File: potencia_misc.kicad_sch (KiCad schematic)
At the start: 68 parts, among them J6 ATX-20, M1 Fan, M2 Fan, M3 Fan, Q1 NMOS, Q10 MMBT2222A, Q11 MMBT2222A, Q12 MMBT2222A, Q13 MMBT2222A, Q14 MMBT2907ALT1G, Q15 MMBT2222A, Q16 MMBT2222A, Q17 MMBT2222A, Q18 MMBT2907ALT1G, Q19 MMBT2222A, Q2 NMOS, Q20 MMBT2907ALT1G, Q3 NMOS, Q4 NMOS, Q9 MMBT2907ALT1G, SW3 SW_Push, U8 TPS54302

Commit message: 10082026/B
nova revisão
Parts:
- removed C59: 10uf, symbol Device:C
- removed C60, C62: 100nf, Capacitor_SMD:C_0603_1608Metric, symbol Device:C
- removed C66, C67: 22µf, Capacitor_SMD:C_0603_1608Metric, symbol Device:C
- removed C93: 47µf, Capacitor_SMD:C_0603_1608Metric_Pad1.08x0.95mm_HandSolder, symbol Device:C
- removed D1: SMF15A, Diode_SMD:D_SMF, symbol Diode:SMF15A
- removed D2: SMF33A, Diode_SMD:D_SMF, symbol Diode:SMF33A
- removed F1: Polyfuse, symbol Device:Polyfuse
- removed J6: ATX-20, Connector_Molex:Molex_Mini-Fit_Jr_5566-20A_2x10_P4.20mm_Vertical, symbol Connector:ATX-20
- removed L1: 6.8uh, Inductor_SMD:L_Bourns_SRP1038C_10.0x10.0mm, symbol Device:L
- removed R42: 100k, symbol Device:R
- removed R43: 22k, symbol Device:R
- removed TP12: TestPoint, TestPoint:TestPoint_Pad_D1.0mm, symbol Connector:TestPoint
- removed U8: TPS54302, Package_TO_SOT_SMD:SOT-23-6, symbol Regulator_Switching:TPS54302
- added C100, C101: 100nf, Capacitor_SMD:C_0603_1608Metric, symbol Device:C
- added C15: 100nf, symbol Device:C_Small
- added C31: 33nf, Capacitor_SMD:C_0402_1005Metric, symbol Device:C_Small
- added C49, C51, C97, C98: 22µf, symbol Device:C
- added D6: SMF33A, Diode_SMD:D_SMF, symbol Diode:SMF33A
- added F9: Polyfuse, symbol Device:Polyfuse
- added J6: ATX-24, Connector_Molex:Molex_Mini-Fit_Jr_5569-24A2_2x12_P4.20mm_Horizontal, symbol Connector:ATX-24
- added JP5: fre, Jumper:SolderJumper-2_P1.3mm_Open_TrianglePad1.0x1.5mm, symbol Jumper:SolderJumper_2_Open
- added L2: 4.7µh, symbol Device:L
- added R88: 100kΩ, symbol Device:R
- added R89: 57.6kΩ, symbol Device:R
- added R90: 10kΩ, symbol Device:R
- added R92: 330, symbol Device:R_Small
- added R93: 30.9kΩ, symbol Device:R_Small
- added U9: TPS62933F, Package_TO_SOT_SMD:SOT-583-8, symbol Regulator_Switching:TPS62933F
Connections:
- net +12V: now also F9.1
- net +3.3V: now also D6.1 (A1)
- net GND: now also C100.2, C101.2, C31.2, C49.2, C51.2, C97.2, C98.2, D6.2 (A2), J6.15 (GND), J6.17 (GND), J6.18 (GND), J6.19 (GND), J6.24 (GND), J6.3 (GND), J6.5 (GND), J6.7 (GND), JP5.1 (A), R89.2, R90.2, U9.4 (GND)
- net SUB_1: now also J6.16 (PS_ON#)
- net hotbed: now also J6.10 (+12V), J6.11 (+12V)
- net at F3.1: now also J6.21 (+5V), J6.22 (+5V), J6.23 (+5V), J6.4 (+5V), J6.6 (+5V)
- new net: R88.2, R89.1, U9.2 (EN)
- new net: C31.1, U9.7 (SS)
- new net: C15.1, U9.6 (BST)
- new net: C15.2, L2.1, U9.5 (SW)
- new net: C101.1, C49.1, C51.1, F9.2, R88.1, U9.3 (VIN)
- new net: JP5.2 (B), U9.1 (RT)
- new net: R92.2, R93.1
- new net: R90.1, R93.2, U9.8 (FB)
- new net: C100.1, C97.1, C98.1, L2.2, R92.1
- new net: J6.1 (+3.3V), J6.12 (+3.3V), J6.13 (+3.3V), J6.2 (+3.3V)
- no-connect marks 5 -> 4
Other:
- company: (none) -> ---
- moved on the sheet: C61, C63, C64, C65, C94, F2, F3, SW3, TP11, TP13, TP14, TP15

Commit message: 10082026/D
"erros bobos"
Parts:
- removed Q10, Q11, Q12, Q13, Q15, Q16, Q17, Q19: MMBT2222A, Package_TO_SOT_SMD:SOT-23, symbol Transistor_BJT:MMBT2222A
- removed Q14, Q18, Q20, Q9: MMBT2907ALT1G, Package_TO_SOT_SMD:SOT-23, symbol Simulation_SPICE:PNP
- removed R76, R81, R86, R87: 39Ω, symbol Device:R
- removed R77, R78, R79, R80, R82, R83, R84, R85: 1kΩ, symbol Device:R
- added C10, C12, C8, C9: 100nf, symbol Device:C
- added Q10, Q11, Q12, Q9: PMOS, symbol Simulation_SPICE:PMOS
- added Q22, Q23, Q24, Q25: NMOS, symbol Simulation_SPICE:NMOS
- added R100, R104, R108, R112: 100, symbol Device:R
- added R101, R105, R109, R113: 220, symbol Device:R
- added R102, R106, R110, R98: 100Ω, symbol Device:R
- added R103, R107, R111, R99: 10k, symbol Device:R
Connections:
- net Fan_2_D is gone; now on net Fan_1_D: Q4.2 (G), R47.1
- net exrtusora_out is gone; now on net Fan_1_D: Q2.2 (G), R45.1
- net +12V: now also R100.2, R104.2, R108.2, R112.2
- net +3.3V: now also C100.1, C97.1, C98.1, L2.2, R92.1
- net Fan_1: now also Q11.2 (G), Q24.2 (G), R106.1, R107.1
- net Fan_1_D: now also C10.2, C12.2, C8.2, C9.2, Q10.3 (S), Q11.3 (S), Q12.3 (S), Q22.1 (D), Q23.1 (D), Q24.1 (D), Q25.1 (D), Q9.3 (S), R101.2, R105.2, R109.2, R113.2
- net Fan_2: now also Q12.2 (G), Q25.2 (G), R110.1, R111.1
- net GND: now also C10.1, C12.1, C8.1, C9.1, Q22.3 (S), Q23.3 (S), Q24.3 (S), Q25.3 (S), R101.1, R102.2, R103.2, R105.1, R106.2, R107.2, R109.1, R110.2, R111.2, R113.1, R98.2, R99.2
- net exrtusora: now also Q10.2 (G), Q23.2 (G), R102.1, R103.1
- net hot_bed: now also Q22.2 (G), Q9.2 (G), R98.1, R99.1
- new net: Q12.1 (D), R112.1
- new net: Q10.1 (D), R104.1
- new net: Q11.1 (D), R108.1
- new net: Q9.1 (D), R100.1
- no-connect marks 4 -> 5

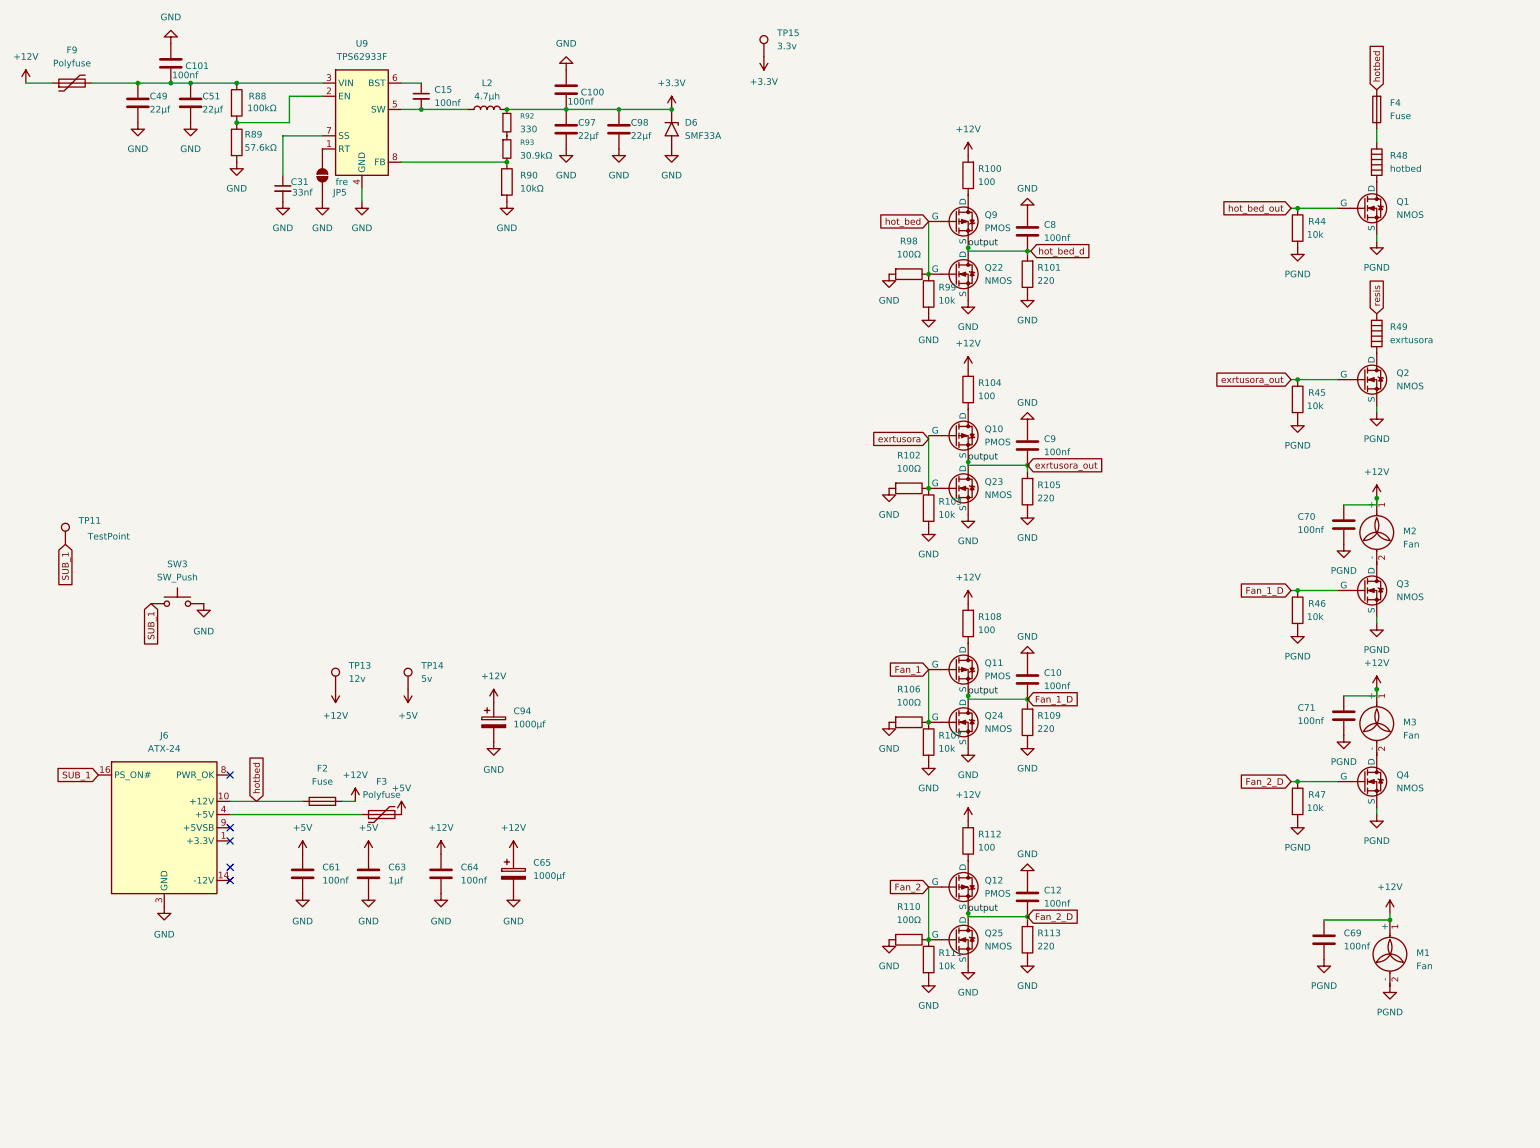
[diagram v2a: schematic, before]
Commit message: 17082026/E
modulo FRAM e Melhoria no esquemático
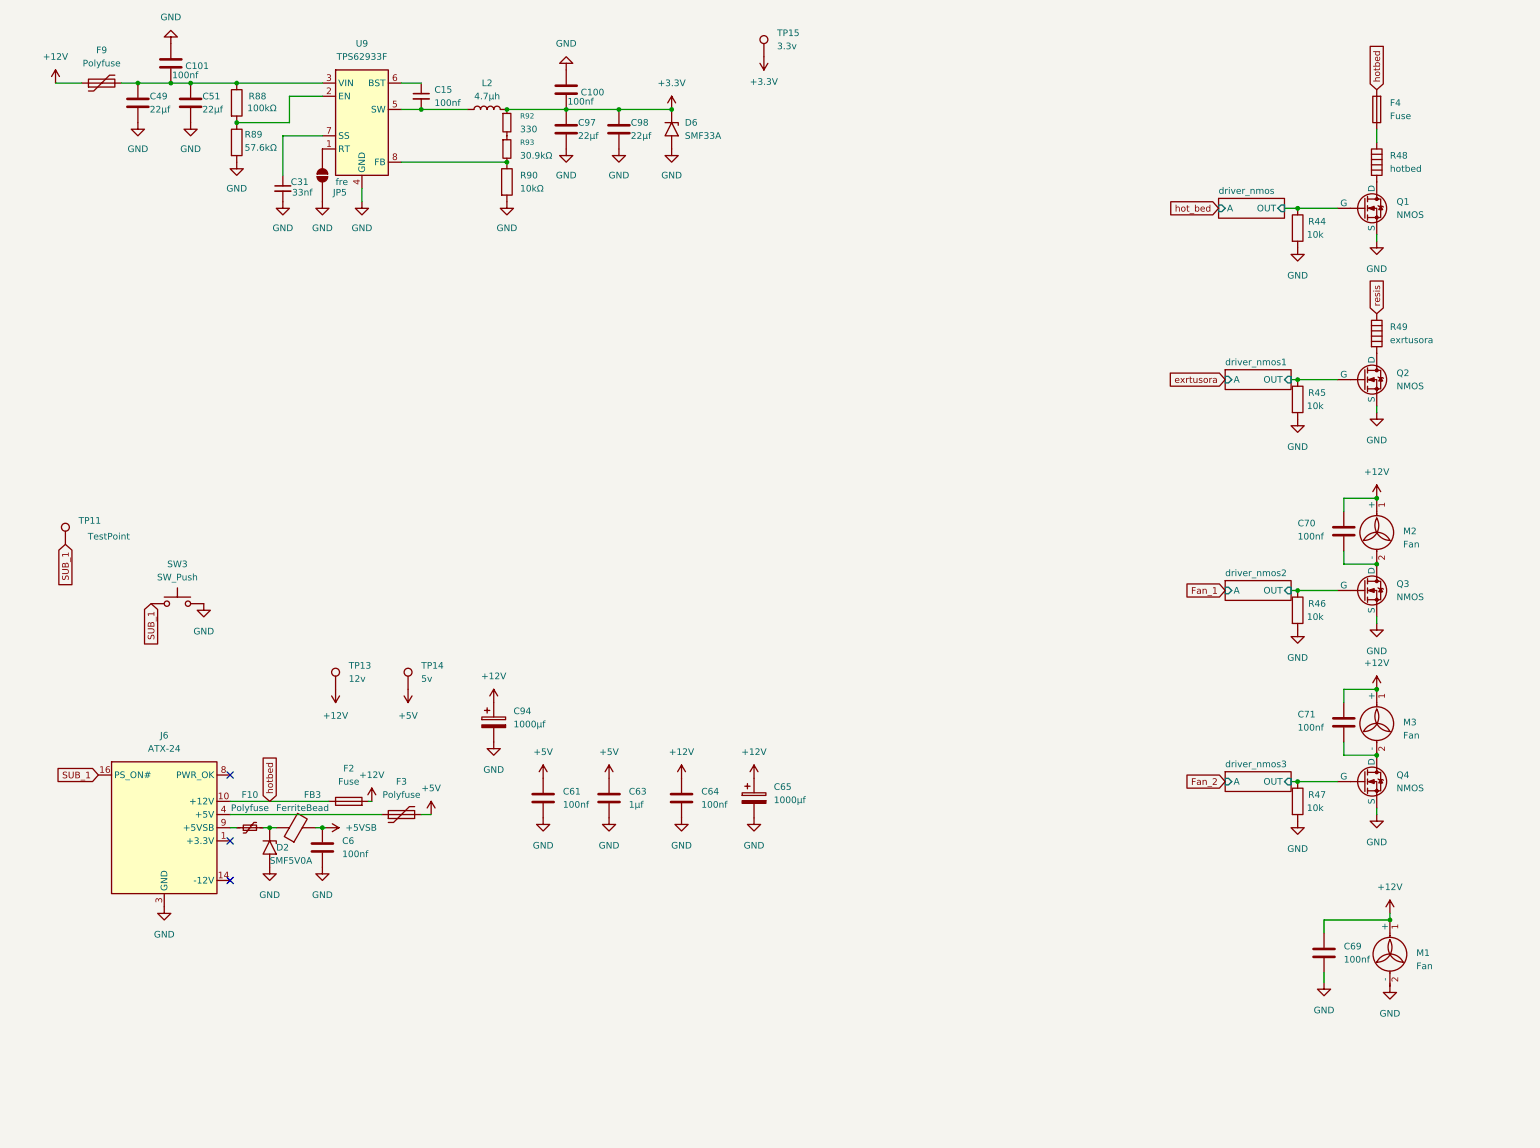
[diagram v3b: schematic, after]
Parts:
- removed C10, C12, C8, C9: 100nf, symbol Device:C
- removed Q10, Q11, Q12, Q9: PMOS, symbol Simulation_SPICE:PMOS
- removed Q22, Q23, Q24, Q25: NMOS, symbol Simulation_SPICE:NMOS
- removed R100, R104, R108, R112: 100, symbol Device:R
- removed R101, R105, R109, R113: 220, symbol Device:R
- removed R102, R106, R110, R98: 100Ω, symbol Device:R
- removed R103, R107, R111, R99: 10k, symbol Device:R
- added C6: 100nf, Capacitor_SMD:C_0603_1608Metric, symbol Device:C
- added D2: SMF5V0A, Diode_SMD:D_SMF, symbol Diode:SMF5V0A
- added F10: Polyfuse, symbol Device:Polyfuse_Small
- added FB3: FerriteBead, Inductor_SMD:L_0805_2012Metric, symbol Device:FerriteBead
- C15: footprint (none) -> Capacitor_SMD:C_0603_1608Metric; jlc_pcb: (none) -> C346191
- C63: footprint (none) -> Capacitor_SMD:C_0805_2012Metric_Pad1.18x1.45mm_HandSolder; jlc_pcb: (none) -> C28323
- J6: Descrição (none) -> entrada de alimentaçao para o harpia ninho 12v, os pinos na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
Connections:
- net GND: now also C69.2, M1.2 (-), Q1.3 (S), Q2.3 (S), Q3.3 (S), Q4.3 (S), R44.2, R45.2, R46.2, R47.2, C6.2, D2.2 (A2)
- net at M2.2 (-), Q3.1 (D): now also C70.2
- net at M3.2 (-), Q4.1 (D): now also C71.2
- net at J6.9 (+5VSB): now also F10.1
- removed net Fan_1_D: Q2.2 (G), Q3.2 (G), Q4.2 (G), R45.1, R46.1, R47.1
- removed net PGND: C69.2, C70.2, C71.2, M1.2 (-), Q1.3 (S), Q2.3 (S), Q3.3 (S), Q4.3 (S), R44.2, R45.2, R46.2, R47.2
- net hot_bed_out renamed driver_nmos/OUT
- new net: D2.1 (A1), F10.2, FB3.1
- new net +5VSB: C6.1, FB3.2
- new net driver_nmos1/OUT: Q2.2 (G), R45.1
- new net driver_nmos2/OUT: Q3.2 (G), R46.1
- new net driver_nmos3/OUT: Q4.2 (G), R47.1
- no-connect marks 5 -> 3
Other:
- added sheet driver_nmos (d-nmos.kicad_sch)
- added sheet driver_nmos1 (d-nmos.kicad_sch)
- added sheet driver_nmos2 (d-nmos.kicad_sch)
- added sheet driver_nmos3 (d-nmos.kicad_sch)
- moved on the sheet: C61, C63, C64, C65, C69, C70, C71, F2, F3, F9

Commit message: 18082026/F
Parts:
- removed D6: SMF33A, Diode_SMD:D_SMF, symbol Diode:SMF33A
- added D7: SMF5V0A, Diode_SMD:D_SMF, symbol Diode:SMF5V0A
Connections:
- net +3.3V: now also D7.1 (A1)
- net GND: now also D7.2 (A2)
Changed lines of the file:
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@@
-	)
-	(symbol
-		(lib_id "Diode:SMF33A")
-		(at 139.7 33.02 270)
-		(unit 1)
-		(body_style 1)
-		(exclude_from_sim no)
-		(in_bom yes)
-		(on_board yes)
-		(in_pos_files yes)
-		(dnp no)
-		(fields_autoplaced yes)
-		(property "Reference" "D6"
-			(at 142.24 31.7499 90)
-			(show_name no)
-			(do_not_autoplace no)
-			(effects
-				(font
-					(size 1.27 1.27)
-				)
-				(justify left)
-			)
-		)
-		(property "Value" "SMF33A"
-			(at 142.24 34.2899 90)
-			(show_name no)
-			(do_not_autoplace no)
-			(effects
-				(font
-					(size 1.27 1.27)
-				)
-				(justify left)
-			)
-		)
-		(property "Footprint" "Diode_SMD:D_SMF"
-			(at 134.62 33.02 0)
-			(hide yes)
-			(show_name no)
-			(do_not_autoplace no)
-			(effects
-				(font
-					(size 1.27 1.27)
-				)
-			)
-		)
-		(property "Datasheet" "https://www.vishay.com/doc?85881"
-			(at 139.7 31.75 0)
-			(hide yes)
-			(show_name no)
-			(do_not_autoplace no)
-			(effects
-				(font
-					(size 1.27 1.27)
-				)
-			)
-		)
-		(property "Description" "200W unidirectional Transil Transient Voltage Suppressor, 33Vrwm, SMF"
-			(at 139.7 33.02 0)
-			(hide yes)
-			(show_name no)
-			(do_not_autoplace no)
-			(effects
-				(font
-					(size 1.27 1.27)
-				)
-			)
-		)
-		(pin "1"
-		)
-		(pin "2"
-		)
-		(instances
-			(project "hapia"
-				(path "/a3449e8f-77d7-48cf-b22a-69e9391d97ed"
-					(reference "D6")
-					(unit 1)
-				)
-			)
-		)
 	)
 	(symbol
@@
 					(unit 1)
 				)
+			)
+		)
+	)
+	(symbol
+		(lib_id "Diode:SMF5V0A")
+		(at 139.7 33.02 270)
+		(unit 1)
+		(body_style 1)
+		(exclude_from_sim no)
+		(in_bom yes)
+		(on_board yes)
+		(in_pos_files yes)
+		(dnp no)
+		(fields_autoplaced yes)
+		(property "Reference" "D7"
+			(at 142.24 31.7499 90)
+			(show_name no)
+			(do_not_autoplace no)
+			(effects
+				(font
+					(size 1.27 1.27)
+				)
+				(justify left)
+			)
+		)
+		(property "Value" "SMF5V0A"
+			(at 142.24 34.2899 90)
+			(show_name no)
+			(do_not_autoplace no)
+			(effects
+				(font
+					(size 1.27 1.27)
+				)
+				(justify left)
+			)
+		)
+		(property "Footprint" "Diode_SMD:D_SMF"
+			(at 134.62 33.02 0)
+			(hide yes)
+			(show_name no)
+			(do_not_autoplace no)
+			(effects
+				(font
+					(size 1.27 1.27)
+				)
+			)
+		)
+		(property "Datasheet" "https://www.vishay.com/doc?85881"
+			(at 139.7 31.75 0)
+			(hide yes)
+			(show_name no)
+			(do_not_autoplace no)
+			(effects
+				(font
+					(size 1.27 1.27)
+				)
+			)
+		)
+		(property "Description" "200W unidirectional Transil Transient Voltage Suppressor, 5Vrwm, SMF"
+			(at 139.7 33.02 0)
+			(hide yes)
+			(show_name no)
+			(do_not_autoplace no)
+			(effects
+				(font
+					(size 1.27 1.27)
+				)
+			)
+		)
+		(pin "2"
+		)
+		(pin "1"
+		)
+		(instances
+			(project "hapia"
+				(path "/a3449e8f-77d7-48cf-b22a-69e9391d97ed"
+					(reference "D7")
+					(unit 1)
+				)

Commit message: 21082026/G
falta muita coisa
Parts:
- added Q1: NMOS, symbol Simulation_SPICE:NMOS
- added R73, R74: 10kΩ, symbol Device:R
- added R75: 1kΩ, symbol Device:R
- renumbered C49 to C53, C101 to C54, C51 to C55, C31 to C56, C6 to C57, C15 to C58, C94 to C59, C61 to C60, C100 to C61, C97 to C62, C98 to C64, C64 to C65, C65 to C66, C69 to C67, C70 to C68, C71 to C69, D2 to D3, D7 to D4, F9 to F4, F10 to F5, F2 to F6, F3 to F7, F4 to F8, J6 to J7, JP5 to JP2, L2 to L1, M2 to M1, M3 to M2, M1 to M3, Q1 to Q2, Q2 to Q3, Q3 to Q4, Q4 to Q5, R88 to R71, R89 to R72, R92 to R76, R93 to R77, R90 to R78, R44 to R79, R45 to R80, R46 to R81, R47 to R82, R48 to R83, R49 to R84, TP11 to TP13, TP13 to TP14, TP14 to TP15, TP15 to TP16, U9 to U8
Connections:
- net +3.3V: now also R75.2
- net GND: now also Q1.3 (S)
- net ATX_PWR: now reaches J7.8 (PWR_OK)
- net ATX_PWR: now also R73.2, R74.1
- new net: Q1.1 (D), R75.1
- new net: Q1.2 (G), R74.2
- no-connect marks 3 -> 2

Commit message: 23082026/H
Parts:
- removed Q1, Q2, Q3: NMOS, symbol Simulation_SPICE:NMOS
- removed R75: 1kΩ, symbol Device:R
- added D11, D12, D8: SMF15A, Diode_SMD:D_SMF, symbol Diode:SMF15A
- added D9: SMF5V0A, Diode_SMD:D_SMF, symbol Diode:SMF5V0A
- added R108, R109: 12, symbol Device:R
- added U11: UCC27524DR, Package_SO:SOIC-8_3.9x4.9mm_P1.27mm, symbol Driver_FET:UCC27524D
- added U12: UCC27524D, Package_SO:SOIC-8_3.9x4.9mm_P1.27mm, symbol Driver_FET:UCC27524D
- added U13, U14: IRFS7530TRL7PP, Package_TO_SOT_SMD:TO-263-7_TabPin4, symbol MOS_S:IRFS7530TRL7PP
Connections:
- net +12V: now also D8.1 (A1), U11.2 (INA), U11.4 (INB), U12.2 (INA), U12.4 (INB)
- net +3.3V: now also U11.6 (V_{DD}), U12.6 (V_{DD})
- net ATX_PWR: now also R74.2; no longer R73.2, R74.1
- net Fan_1: now also U11.1 (ENA)
- net Fan_2: now also U11.8 (ENB)
- net GND: now also R73.1, D11.2 (A2), D12.2 (A2), D8.2 (A2), D9.2 (A2), U11.3 (GND), U12.3 (GND), U13.2 (S), U13.3 (S), U13.5 (S), U13.6 (S), U13.7 (S), U14.2 (S), U14.3 (S), U14.5 (S), U14.6 (S), U14.7 (S)
- net exrtusora: now also U12.8 (ENB)
- net hot_bed: now also U12.1 (ENA)
- net at R83.2: now also U13.4 (D)
- net at R84.2: now also U14.4 (D)
- net driver_nmos/OUT: no longer names the net of R79.1
- net driver_nmos/OUT: now also D12.1 (A1), R108.2, U13.1 (G)
- net driver_nmos1/OUT: no longer names the net of R80.1
- net driver_nmos1/OUT: now also D11.1 (A1), R109.2, U14.1 (G)
- net driver_nmos2/OUT: no longer names the net of Q4.2 (G), R81.1
- net driver_nmos2/OUT: now also U11.7 (OUTA)
- net driver_nmos3/OUT: no longer names the net of Q5.2 (G), R82.1
- net driver_nmos3/OUT: now also U11.5 (OUTB)
- new net: R109.1, U12.5 (OUTB)
- new net: R108.1, U12.7 (OUTA)
- new net ATX_PWR_o: D9.1 (A1), R73.2, R74.1
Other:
- removed sheet driver_nmos
- removed sheet driver_nmos1
- removed sheet driver_nmos2
- removed sheet driver_nmos3
- moved on the sheet: R74, R79, R80, R82

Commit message: 29082026/I
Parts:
- removed D11, D12: SMF15A, Diode_SMD:D_SMF, symbol Diode:SMF15A
- C54, C60, C61, C65, C67, C68, C69: jlc_pcb: C346191 -> C307348; mouser: (none) -> 187-CL10B104KB8WPNC; mpn CL10B104KB8NFNC -> CL10B104KB8WPNC
- C57, C58: jlc_pcb: C346191 -> C307348; mouser: (none) -> 187-CL10B104KB8WPNC; mpn (none) -> CL10B104KB8WPNC
- D4: value SMF5V0A -> SMF3.3
- J7: mouser: (none) -> 538-39-30-1240
- L1: footprint (none) -> Inductor_SMD:L_Changjiang_FNR6020S; jlc_pcb: (none) -> C307880; mouser: (none) -> 810-VLS6045EX-4R7M; mpn (none) -> VLS6045EX-4R7M
- U11: mouser: (none) -> 595-UCC27524DR
- U12: value UCC27524D -> UCC27524DR; jlc_pcb: (none) -> C465729; mouser: (none) -> 595-UCC27524DR; mpn (none) -> UCC27524DR
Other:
- moved on the sheet: D9, R73, R74

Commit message: o .bom não foi terminado
O desafio e todo custar menos de 150 dólares(eua) e menos de 1000r(reais)
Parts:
- removed D8: SMF15A, Diode_SMD:D_SMF, symbol Diode:SMF15A
- removed D9: SMF5V0A, Diode_SMD:D_SMF, symbol Diode:SMF5V0A
- added D10: SMF12A, Diode_SMD:D_SMF, symbol Diode:SMF12A
- added D8: SMF3.3, Diode_SMD:D_SMF, symbol Diode:SMF5V0A
- C53, C55, C62, C64: footprint (none) -> Capacitor_SMD:C_0805_2012Metric_Pad1.18x1.45mm_HandSolder; jlc_pcb: (none) -> C86816; mouser: (none) -> 81-GRM21BR61E226ME4L; mpn (none) -> GRM21BR61E226ME44L
- C56: mouser: (none) -> 81-GCM155R71E333KA5D
- C59, C66: mouser: (none) -> 232-35YXJ1000M125X20; mpn (none) -> 35YXJ1000M12.5X20
- C63: mouser: (none) -> 187-CL21B105KBFNNNE; mpn (none) -> CL21B105KBFNNNE
- R108, R109: value 12 -> 12Ω; footprint (none) -> Resistor_SMD:R_MELF_MMB-0207; jlc_pcb: (none) -> C2078923; mouser: (none) -> 594-MMB02070C1209FB2; mpn (none) -> MMB02070C1209FB200
- R71: footprint (none) -> Resistor_SMD:R_0603_1608Metric_Pad0.98x0.95mm_HandSolder; jlc_pcb: (none) -> C122538; mouser: (none) -> 603-RT0603BRD07100KL; mpn (none) -> RT0603BRD07100KL
- R72: footprint (none) -> Resistor_SMD:R_0402_1005Metric_Pad0.72x0.64mm_HandSolder; jlc_pcb: (none) -> C445587; mouser: (none) -> 667-ERA-2AEB331X; mpn (none) -> ERA2AEB331X
- R76: value 330 -> 330Ω; footprint (none) -> Resistor_SMD:R_0402_1005Metric_Pad0.72x0.64mm_HandSolder; jlc_pcb: (none) -> C445587; mouser: (none) -> 667-ERA-2AEB331X; mpn (none) -> ERA2AEB331X
- R77: footprint (none) -> Resistor_SMD:R_0603_1608Metric_Pad0.98x0.95mm_HandSolder; jlc_pcb: (none) -> C861313; mouser: (none) -> 603-RT0603BRD0730K9L; mpn (none) -> RT0603BRD0730K9L
- R79, R80, R81, R82: value 10k -> 10kΩ
- SW3: footprint (none) -> Connector_PinHeader_2.54mm:PinHeader_1x02_P2.54mm_Vertical; jlc_pcb: (none) -> C234182; mouser: (none) -> 538-22-28-4020; mpn (none) -> 22284020
- TP13, TP14, TP15, TP16: now left out of the parts list
- U13, U14: jlc_pcb: (none) -> C445669; mouser: (none) -> 942-IRFS7530TRL7PP; mpn (none) -> IRFS7530TRL7PP
- U8: mouser: (none) -> 595-TPS62933FDRLR
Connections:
- net +12V: now also D10.1 (A1)
- net ATX_PWR_o: now also D8.1 (A1)
- net GND: now also D10.2 (A2), D8.2 (A2)
